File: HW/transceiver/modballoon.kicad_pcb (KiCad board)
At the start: 4 copper layers, 152 parts, among them K1 CONN_6, K2 CONN_10, K3 CONN_6, K4 CONN_6, K5 SMA, K6 SMA, K7 HE10-20, K8 SAM_JTAG, M1 CONN_01X01, M2 CONN_01X01, M3 CONN_01X01, M4 CONN_01X01, M5 CONN_01X01, M6 CONN_01X01, M7 CONN_01X01, M8 CONN_01X01, X1 FA-238V-12MHZ, X2 7Q-26.000MBN-T

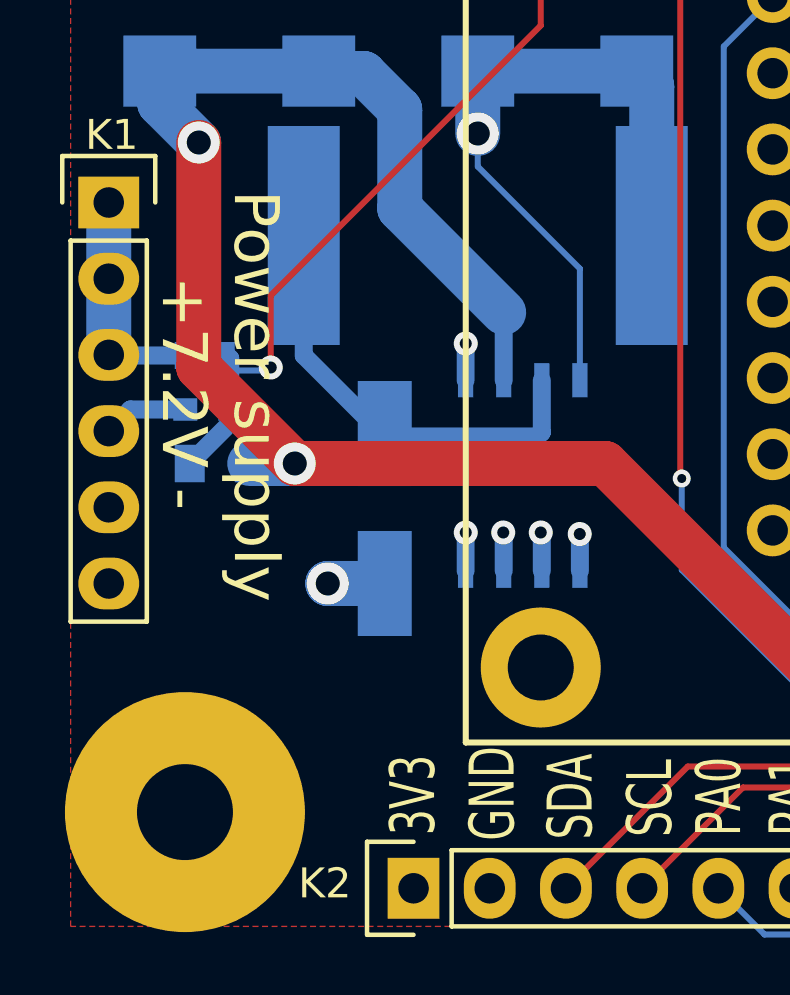
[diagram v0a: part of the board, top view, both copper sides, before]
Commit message: new protection feature - inverted power supply protection diode.
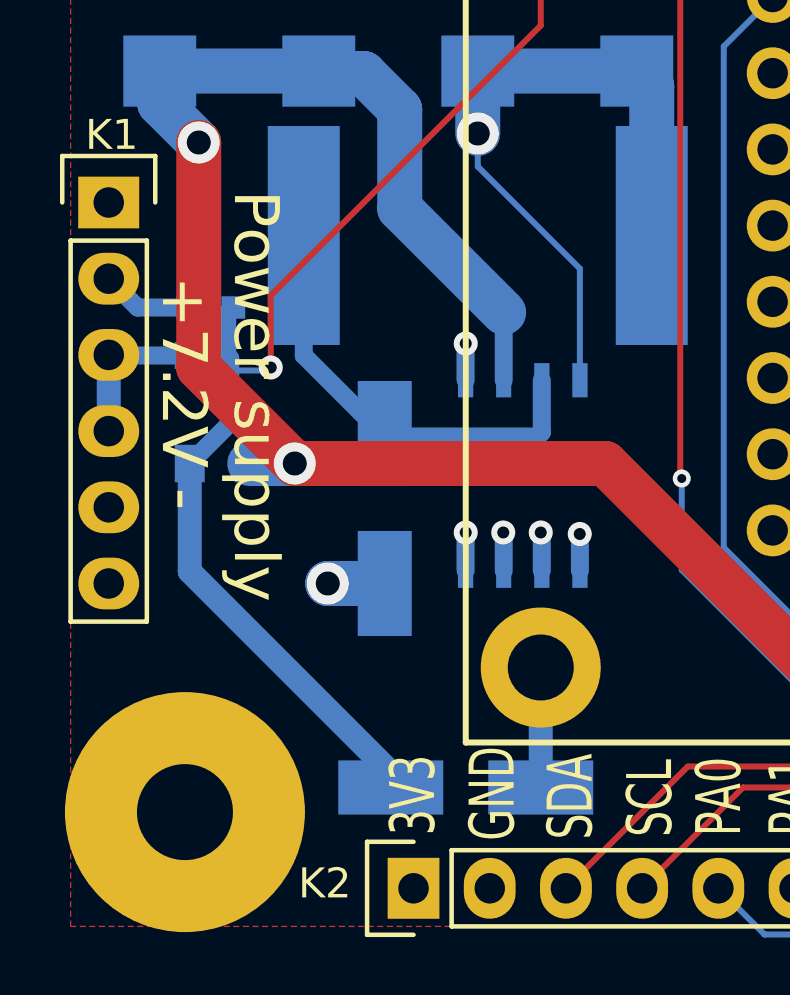
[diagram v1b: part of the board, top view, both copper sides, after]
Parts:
- added D3: B260A, Diodes_SMD:SMA_Handsoldering, B.Cu at (50.0, 146.5)
- moved C3 3.40 mm to (41.5, 130.5)
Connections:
- K1 pad 1: Net-(F1-Pad1) -> GND
- K1 pad 2: Net-(F1-Pad1) -> GND
- K1 pad 4: GND -> Net-(F1-Pad1)
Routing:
- net /Microcontroller/Vbat: track 46.1 -> 61.3 mm
- net Net-(F1-Pad1): track 10.1 -> 5.00 mm
- net GND: track 137.2 -> 141.4 mm
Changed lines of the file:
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@@
 (kicad_pcb (version 4) (host pcbnew 4.0.2+e4-6225~38~ubuntu14.04.1-stable)
   (general
-    (links 374)
+    (links 376)
     (no_connects 0)
-    (area 34.906429 97.994048 155.32 165.260001)
+    (area 0 0 0 0)
     (thickness 1.6)
     (drawings 55)
-    (tracks 1166)
+    (tracks 1172)
     (zones 0)
-    (modules 152)
+    (modules 153)
     (nets 142)
   )
   (page A4)
   (layers
-    (0 F.Cu signal hide)
+    (0 F.Cu signal)
     (1 In1.Cu signal hide)
     (2 In2.Cu signal hide)
-    (31 B.Cu signal hide)
-    (32 B.Adhes user hide)
-    (33 F.Adhes user hide)
+    (31 B.Cu signal)
+    (32 B.Adhes user)
+    (33 F.Adhes user)
     (34 B.Paste user hide)
-    (35 F.Paste user hide)
+    (35 F.Paste user)
     (36 B.SilkS user hide)
     (37 F.SilkS user hide)
@@
   )
   (setup
-    (last_trace_width 0.2)
+    (last_trace_width 0.6)
     (user_trace_width 0.2)
     (user_trace_width 0.2)
@@
     (pad_to_mask_clearance 0)
     (aux_axis_origin 0 0)
-    (visible_elements FFFEF6E9)
+    (visible_elements FFFEF6FF)
     (pcbplotparams
       (layerselection 0x00030_80000001)
@@
   )
   (module Capacitors_SMD:C_0603 (layer B.Cu)
-    (at 41.4 133.9 180)
+    (at 41.5 130.5 180)
     (descr "Capacitor SMD 0603, reflow soldering, AVX (see smccp.pdf)")
     (tags "capacitor 0603")
@@
     (fp_line (start -1.55 -1.55) (end 1.55 -1.55) (layer F.SilkS) (width 0.15))
     (pad 1 thru_hole rect (at 0 0) (size 2.032 1.7272) (drill 1.016) (layers *.Cu *.Mask F.SilkS)
-      (net 113 "Net-(F1-Pad1)"))
+      (net 2 GND))
     (pad 2 thru_hole oval (at 0 2.54) (size 2.032 1.7272) (drill 1.016) (layers *.Cu *.Mask F.SilkS)
-      (net 113 "Net-(F1-Pad1)"))
+      (net 2 GND))
     (pad 3 thru_hole oval (at 0 5.08) (size 2.032 1.7272) (drill 1.016) (layers *.Cu *.Mask F.SilkS)
       (net 113 "Net-(F1-Pad1)"))
     (pad 4 thru_hole oval (at 0 7.62) (size 2.032 1.7272) (drill 1.016) (layers *.Cu *.Mask F.SilkS)
-      (net 2 GND))
+      (net 113 "Net-(F1-Pad1)"))
     (pad 5 thru_hole oval (at 0 10.16) (size 2.032 1.7272) (drill 1.016) (layers *.Cu *.Mask F.SilkS)
       (net 2 GND))
@@
       (net 2 GND))
   )
+  (module Diodes_SMD:SMA_Handsoldering (layer B.Cu)
+    (at 50 146.5)
+    (descr "Diode SMA Handsoldering")
+    (tags "Diode SMA Handsoldering")
+    (attr smd)
+    (fp_text reference D3 (at 0 2.85) (layer B.SilkS)
+      (effects (font (size 1 1) (thickness 0.15)) (justify mirror))
+    )
+    (fp_text value B260A (at 0.05 -4.4) (layer B.Fab)
+      (effects (font (size 1 1) (thickness 0.15)) (justify mirror))
+    )
+    (fp_line (start -4.5 2) (end 4.5 2) (layer B.CrtYd) (width 0.05))
+    (fp_line (start 4.5 2) (end 4.5 -2) (layer B.CrtYd) (width 0.05))
+    (fp_line (start 4.5 -2) (end -4.5 -2) (layer B.CrtYd) (width 0.05))
+    (fp_line (start -4.5 -2) (end -4.5 2) (layer B.CrtYd) (width 0.05))
+    (fp_line (start -0.25 0) (end 0.3 0.45) (layer B.SilkS) (width 0.15))
+    (fp_line (start 0.3 0.45) (end 0.3 -0.45) (layer B.SilkS) (width 0.15))
+    (fp_line (start 0.3 -0.45) (end -0.25 0) (layer B.SilkS) (width 0.15))
+    (fp_line (start -0.25 0.55) (end -0.25 -0.55) (layer B.SilkS) (width 0.15))
+    (fp_text user K (at -3.25 -2.9) (layer B.SilkS)
+      (effects (font (size 1 1) (thickness 0.15)) (justify mirror))
+    )
+    (fp_text user A (at 3.05 -2.85) (layer B.SilkS)
+      (effects (font (size 1 1) (thickness 0.15)) (justify mirror))
+    )
+    (fp_line (start -1.79914 -1.75006) (end -1.79914 -1.39954) (layer B.SilkS) (width 0.15))
+    (fp_line (start -1.79914 1.75006) (end -1.79914 1.39954) (layer B.SilkS) (width 0.15))
+    (fp_line (start 2.25044 -1.75006) (end 2.25044 -1.39954) (layer B.SilkS) (width 0.15))
+    (fp_line (start -2.25044 -1.75006) (end -2.25044 -1.39954) (layer B.SilkS) (width 0.15))
+    (fp_line (start -2.25044 1.75006) (end -2.25044 1.39954) (layer B.SilkS) (width 0.15))
+    (fp_line (start 2.25044 1.75006) (end 2.25044 1.39954) (layer B.SilkS) (width 0.15))
+    (fp_line (start -2.25044 -1.75006) (end 2.25044 -1.75006) (layer B.SilkS) (width 0.15))
+    (fp_line (start -2.25044 1.75006) (end 2.25044 1.75006) (layer B.SilkS) (width 0.15))
+    (pad 1 smd rect (at -2.49936 0) (size 3.50012 1.80086) (layers B.Cu B.Paste B.Mask)
+      (net 4 /Microcontroller/Vbat))
+    (pad 2 smd rect (at 2.49936 0) (size 3.50012 1.80086) (layers B.Cu B.Paste B.Mask)
+      (net 2 GND))
+    (model Diodes_SMD.3dshapes/SMA_Handsoldering.wrl
+      (at (xyz 0 0 0))
+      (scale (xyz 0.3937 0.3937 0.3937))
+      (rotate (xyz 0 0 180))
+    )
+  )
   (gr_line (start 50 145) (end 50 110) (angle 90) (layer F.SilkS) (width 0.2))
   (gr_line (start 125 145) (end 50 145) (angle 90) (layer F.SilkS) (width 0.2))
@@
   (segment (start 62.81 130.35) (end 64.9 130.35) (width 0.6) (layer B.Cu) (net 1))
   (segment (start 60.23 130.31) (end 62.77 130.31) (width 0.6) (layer B.Cu) (net 1))
+  (segment (start 40.75 130.5) (end 39.06 130.5) (width 0.6) (layer B.Cu) (net 2))
+  (segment (start 39.06 130.5) (end 38.1 129.54) (width 0.6) (layer B.Cu) (net 2))
+  (segment (start 52.49936 146.5) (end 52.49936 142.50064) (width 0.8) (layer B.Cu) (net 2))
+  (segment (start 52.49936 142.50064) (end 52.5 142.5) (width 0.8) (layer B.Cu) (net 2))
   (segment (start 99.5 121.4) (end 100.25 121.4) (width 0.2) (layer B.Cu) (net 2))
   (via (at 99.5 121.4) (size 0.8) (drill 0.4) (layers F.Cu B.Cu) (net 2))
@@
   (via (at 45.4 139.7) (size 1.4) (drill 0.8) (layers F.Cu B.Cu) (net 2))
   (segment (start 45.40064 139.69936) (end 45.4 139.7) (width 1.5) (layer B.Cu) (net 2))
-  (segment (start 40.65 133.9) (end 38.82 133.9) (width 0.6) (layer B.Cu) (net 2))
-  (segment (start 38.82 133.9) (end 38.1 134.62) (width 0.6) (layer B.Cu) (net 2))
   (segment (start 49.995 132.925) (end 49.995 131.705) (width 0.6) (layer B.Cu) (net 2))
   (via (at 50 131.7) (size 0.8) (drill 0.4) (layers F.Cu B.Cu) (net 2))
@@
   (segment (start 121.5 128.9556) (end 121.5 129.7) (width 0.2) (layer B.Cu) (net 3))
   (via (at 121.5 129.7) (size 0.8) (drill 0.4) (layers F.Cu B.Cu) (net 3))
+  (segment (start 42.05 132.1) (end 42.05 130.7) (width 0.6) (layer B.Cu) (net 4))
+  (segment (start 42.05 130.7) (end 42.25 130.5) (width 0.6) (layer B.Cu) (net 4))
+  (segment (start 47.50064 146.5) (end 47.50064 146.00064) (width 0.8) (layer B.Cu) (net 4))
+  (segment (start 47.50064 146.00064) (end 40.8 139.3) (width 0.8) (layer B.Cu) (net 4))
+  (segment (start 40.8 139.3) (end 40.8 135.7) (width 0.8) (layer B.Cu) (net 4))
   (segment (start 71.6 110.75) (end 70.55 110.75) (width 0.2) (layer B.Cu) (net 4))
   (segment (start 43.4 132.6) (end 42.15 132.6) (width 0.2) (layer B.Cu) (net 4))
@@
   (segment (start 116.2 130.95) (end 116.2 129.6528) (width 0.6) (layer B.Cu) (net 112))
   (segment (start 116.2 129.6528) (end 116.14834 129.60114) (width 0.6) (layer B.Cu) (net 112))
-  (segment (start 38.1 127) (end 38.1 129.54) (width 0.6) (layer B.Cu) (net 113))
-  (segment (start 38.1 127) (end 38.1 132.08) (width 1.5) (layer B.Cu) (net 113))
+  (segment (start 38.1 134.62) (end 38.1 132.08) (width 0.8) (layer B.Cu) (net 113))
   (segment (start 38.1 132.08) (end 38.12 132.1) (width 0.6) (layer B.Cu) (net 113))
   (segment (start 38.12 132.1) (end 40.55 132.1) (width 0.6) (layer B.Cu) (net 113))

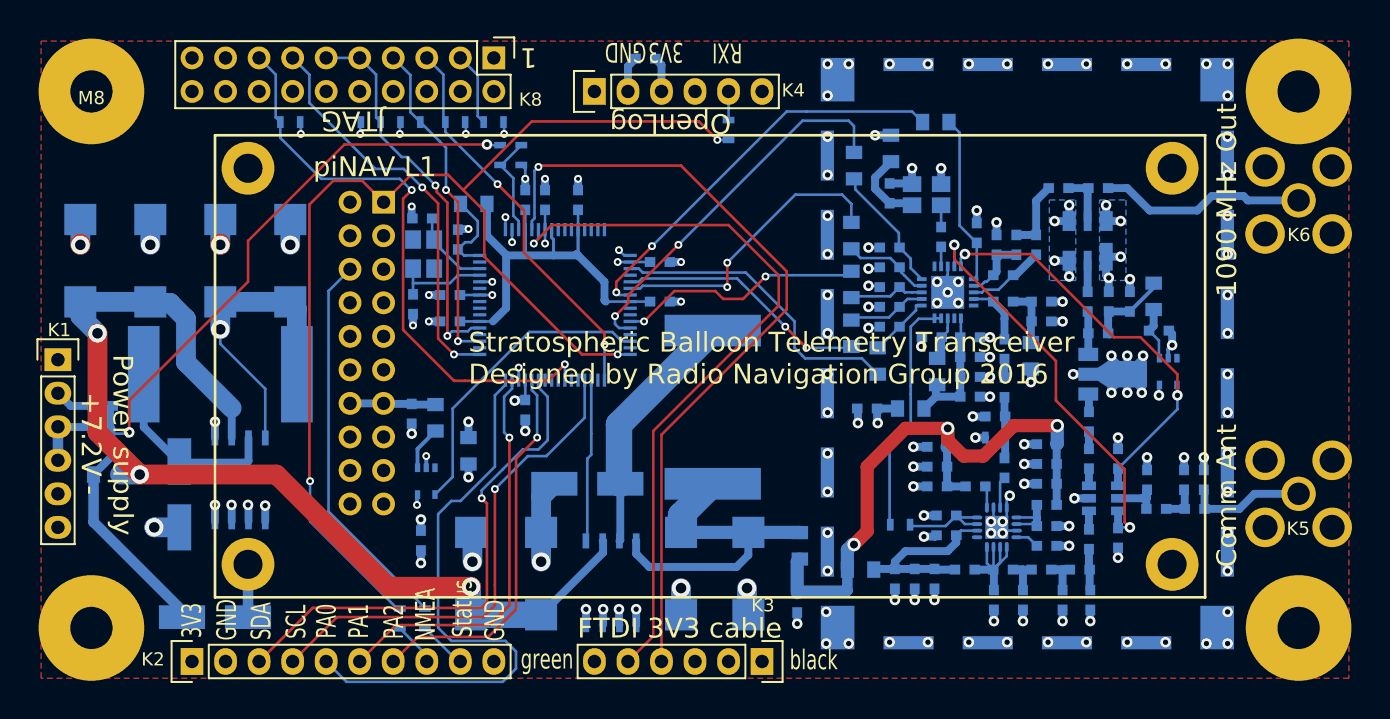
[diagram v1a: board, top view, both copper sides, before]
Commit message: PCB modifications
Modification of dimensions PCB
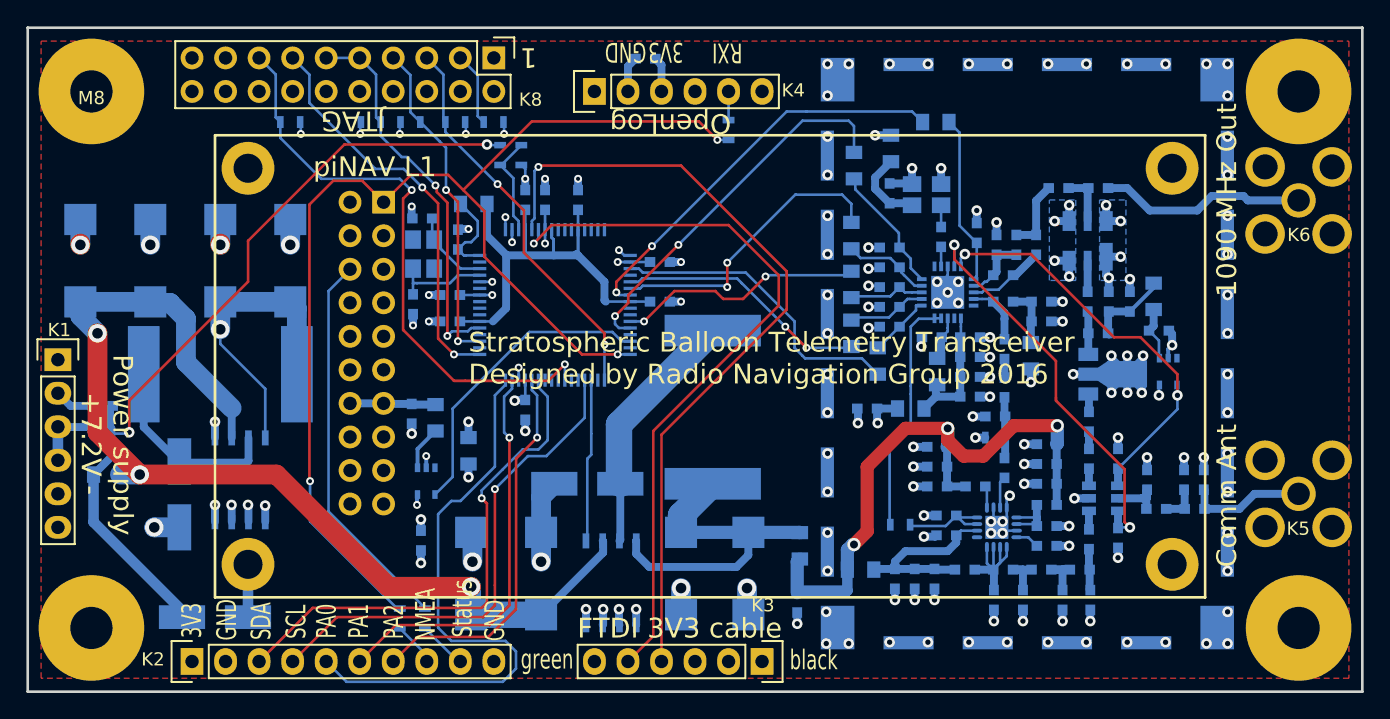
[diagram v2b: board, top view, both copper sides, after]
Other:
- board outline added: 101.1 x 50.3 mm
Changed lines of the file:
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@@
-(kicad_pcb (version 4) (host pcbnew 4.0.2+e4-6225~38~ubuntu14.04.1-stable)
+(kicad_pcb (version 4) (host pcbnew 4.0.3-stable)
   (general
     (links 376)
     (no_connects 0)
-    (area 0 0 0 0)
+    (area 35.713999 101.753999 137.006001 152.246001)
     (thickness 1.6)
     (drawings 55)
@@
   (page A4)
   (layers
-    (0 F.Cu signal)
-    (1 In1.Cu signal hide)
+    (0 F.Cu signal hide)
+    (1 In1.Cu signal)
     (2 In2.Cu signal hide)
-    (31 B.Cu signal)
+    (31 B.Cu signal hide)
     (32 B.Adhes user)
     (33 F.Adhes user)
-    (34 B.Paste user hide)
+    (34 B.Paste user)
     (35 F.Paste user)
-    (36 B.SilkS user hide)
-    (37 F.SilkS user hide)
-    (38 B.Mask user hide)
+    (36 B.SilkS user)
+    (37 F.SilkS user)
+    (38 B.Mask user)
     (39 F.Mask user)
-    (40 Dwgs.User user hide)
-    (41 Cmts.User user hide)
-    (42 Eco1.User user hide)
-    (43 Eco2.User user hide)
+    (40 Dwgs.User user)
+    (41 Cmts.User user)
+    (42 Eco1.User user)
+    (43 Eco2.User user)
     (44 Edge.Cuts user)
     (45 Margin user)
-    (46 B.CrtYd user hide)
-    (47 F.CrtYd user hide)
-    (48 B.Fab user hide)
+    (46 B.CrtYd user)
+    (47 F.CrtYd user)
+    (48 B.Fab user)
     (49 F.Fab user)
   )
   (setup
-    (last_trace_width 0.6)
+    (last_trace_width 0.2)
     (user_trace_width 0.2)
     (user_trace_width 0.2)
@@
     (trace_min 0.2)
     (segment_width 0.2)
-    (edge_width 0.1)
+    (edge_width 0.2)
     (via_size 0.6)
     (via_drill 0.3)
@@
     (pad_to_mask_clearance 0)
     (aux_axis_origin 0 0)
-    (visible_elements FFFEF6FF)
+    (visible_elements 7FFFFFFF)
     (pcbplotparams
       (layerselection 0x00030_80000001)
@@
     )
   )
+  (dimension 50.8 (width 0.3) (layer Dwgs.User)
+    (gr_text "50,800 mm" (at 148.67 127 270) (layer Dwgs.User)
+      (effects (font (size 1.5 1.5) (thickness 0.3)))
+    )
+    (feature1 (pts (xy 142.24 152.4) (xy 150.02 152.4)))
+    (feature2 (pts (xy 142.24 101.6) (xy 150.02 101.6)))
+    (crossbar (pts (xy 147.32 101.6) (xy 147.32 152.4)))
+    (arrow1a (pts (xy 147.32 152.4) (xy 146.733579 151.273496)))
+    (arrow1b (pts (xy 147.32 152.4) (xy 147.906421 151.273496)))
+    (arrow2a (pts (xy 147.32 101.6) (xy 146.733579 102.726504)))
+    (arrow2b (pts (xy 147.32 101.6) (xy 147.906421 102.726504)))
+  )
+  (dimension 101.6 (width 0.3) (layer Dwgs.User)
+    (gr_text "101,600 mm" (at 86.36 163.91) (layer Dwgs.User)
+      (effects (font (size 1.5 1.5) (thickness 0.3)))
+    )
+    (feature1 (pts (xy 137.16 157.48) (xy 137.16 165.26)))
+    (feature2 (pts (xy 35.56 157.48) (xy 35.56 165.26)))
+    (crossbar (pts (xy 35.56 162.56) (xy 137.16 162.56)))
+    (arrow1a (pts (xy 137.16 162.56) (xy 136.033496 163.146421)))
+    (arrow1b (pts (xy 137.16 162.56) (xy 136.033496 161.973579)))
+    (arrow2a (pts (xy 35.56 162.56) (xy 36.686504 163.146421)))
+    (arrow2b (pts (xy 35.56 162.56) (xy 36.686504 161.973579)))
+  )
   (gr_line (start 50 145) (end 50 110) (angle 90) (layer F.SilkS) (width 0.2))
   (gr_line (start 125 145) (end 50 145) (angle 90) (layer F.SilkS) (width 0.2))
@@
     (effects (font (size 1.5 1.5) (thickness 0.3)))
   )
-  (dimension 50.8 (width 0.3) (layer Dwgs.User)
-    (gr_text "50,800 mm" (at 148.67 127 270) (layer Dwgs.User)
-      (effects (font (size 1.5 1.5) (thickness 0.3)))
-    )
-    (feature1 (pts (xy 142.24 152.4) (xy 150.02 152.4)))
-    (feature2 (pts (xy 142.24 101.6) (xy 150.02 101.6)))
-    (crossbar (pts (xy 147.32 101.6) (xy 147.32 152.4)))
-    (arrow1a (pts (xy 147.32 152.4) (xy 146.733579 151.273496)))
-    (arrow1b (pts (xy 147.32 152.4) (xy 147.906421 151.273496)))
-    (arrow2a (pts (xy 147.32 101.6) (xy 146.733579 102.726504)))
-    (arrow2b (pts (xy 147.32 101.6) (xy 147.906421 102.726504)))
-  )
-  (dimension 101.6 (width 0.3) (layer Dwgs.User)
-    (gr_text "101,600 mm" (at 86.36 163.91) (layer Dwgs.User)
-      (effects (font (size 1.5 1.5) (thickness 0.3)))
-    )
-    (feature1 (pts (xy 137.16 157.48) (xy 137.16 165.26)))
-    (feature2 (pts (xy 35.56 157.48) (xy 35.56 165.26)))
-    (crossbar (pts (xy 35.56 162.56) (xy 137.16 162.56)))
-    (arrow1a (pts (xy 137.16 162.56) (xy 136.033496 163.146421)))
-    (arrow1b (pts (xy 137.16 162.56) (xy 136.033496 161.973579)))
-    (arrow2a (pts (xy 35.56 162.56) (xy 36.686504 163.146421)))
-    (arrow2b (pts (xy 35.56 162.56) (xy 36.686504 161.973579)))
-  )
   (gr_line (start 35.814 152.146) (end 35.814 101.854) (angle 90) (layer Margin) (width 0.2))
   (gr_line (start 136.906 152.146) (end 35.814 152.146) (angle 90) (layer Margin) (width 0.2))
@@
   (gr_line (start 45.72 142.24) (end 45.72 149.86) (angle 90) (layer Dwgs.User) (width 0.2))
   (gr_line (start 35.56 142.24) (end 45.72 142.24) (angle 90) (layer Dwgs.User) (width 0.2))
-  (gr_line (start 35.56 101.6) (end 35.56 152.4) (angle 90) (layer Dwgs.User) (width 0.2))
-  (gr_line (start 137.16 101.6) (end 35.56 101.6) (angle 90) (layer Dwgs.User) (width 0.2))
-  (gr_line (start 137.16 152.4) (end 137.16 101.6) (angle 90) (layer Dwgs.User) (width 0.2))
-  (gr_line (start 35.56 152.4) (end 137.16 152.4) (angle 90) (layer Dwgs.User) (width 0.2))
+  (gr_line (start 35.814 101.854) (end 35.814 152.146) (angle 90) (layer Edge.Cuts) (width 0.2))
+  (gr_line (start 136.906 101.854) (end 35.814 101.854) (angle 90) (layer Edge.Cuts) (width 0.2))
+  (gr_line (start 136.906 152.146) (end 136.906 101.854) (angle 90) (layer Edge.Cuts) (width 0.2))
+  (gr_line (start 35.814 152.146) (end 136.906 152.146) (angle 90) (layer Edge.Cuts) (width 0.2))
   (gr_line (start 132.08 149.86) (end 132.08 144.78) (angle 90) (layer Dwgs.User) (width 0.2))
   (gr_line (start 129.54 147.32) (end 134.62 147.32) (angle 90) (layer Dwgs.User) (width 0.2))
